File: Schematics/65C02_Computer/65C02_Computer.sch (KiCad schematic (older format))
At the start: 34 parts

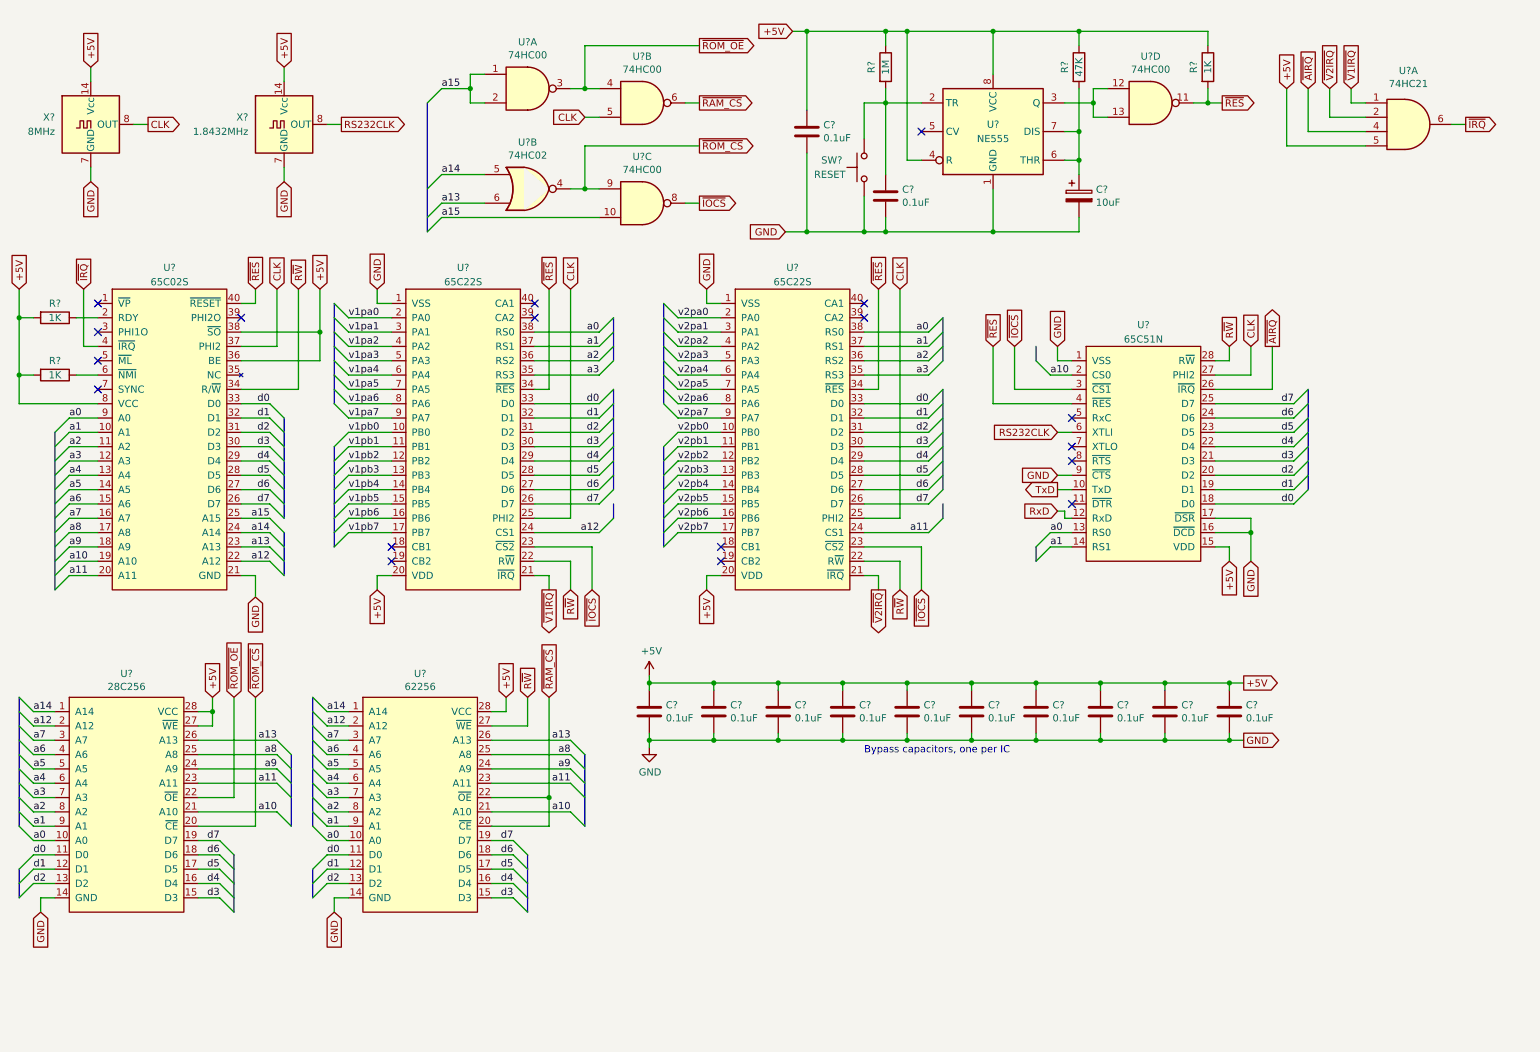
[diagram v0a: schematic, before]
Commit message: Added FT230X chip, moved peripherals to separate sheet
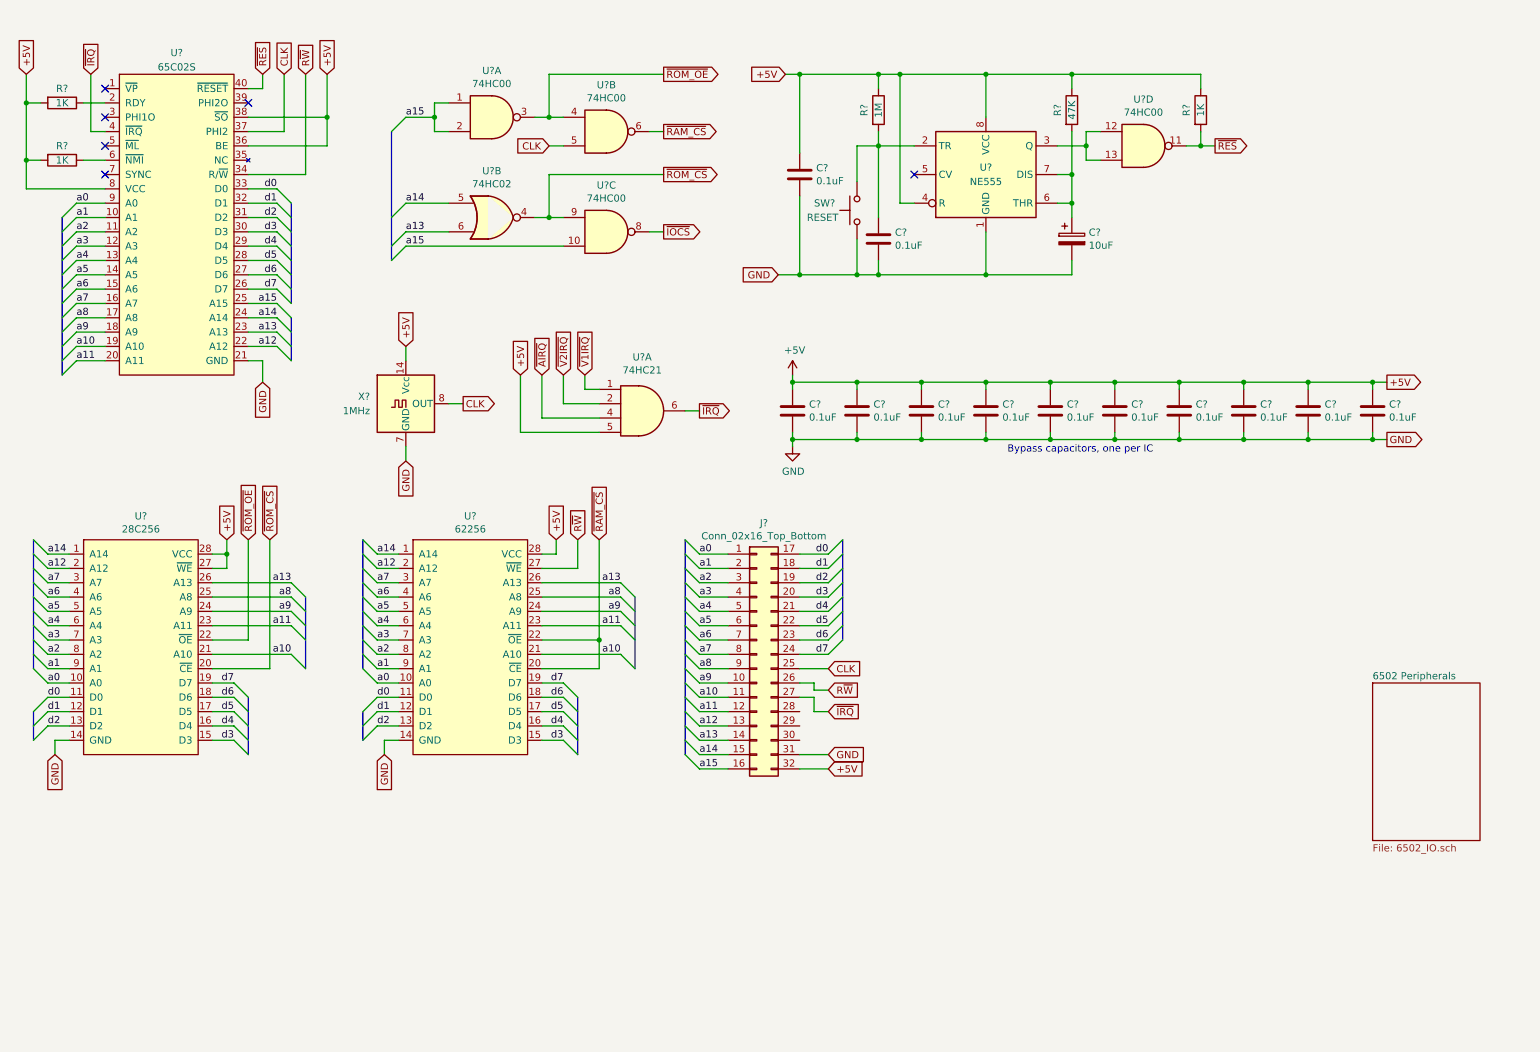
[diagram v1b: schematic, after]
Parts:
- removed U? (x2): 65C22S, Package_DIP:DIP-40_W15.24mm_Socket, symbol 6502:65C22S
- removed U?: 65C51N, Package_DIP:DIP-28_W15.24mm_Socket, symbol 6502:65C51N
- removed X?: 1.8432MHz, Oscillator:Oscillator_DIP-14, symbol Oscillator:ACO-xxxMHz
- added J?: Conn_02x16_Top_Bottom, Connector_PinSocket_2.54mm:PinSocket_2x16_P2.54mm_Vertical, symbol Connector_Generic:Conn_02x16_Top_Bottom
- X?: value 8MHz -> 1MHz
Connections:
- net +5V: now also J?.32 (Pin_32)
- net CLK: now also J?.25 (Pin_25)
- net GND: now also J?.31 (Pin_31)
- net R~W: now also J?.26 (Pin_26)
- net a0: now also J?.1 (Pin_1)
- net a1: now also J?.2 (Pin_2)
- net a10: now also J?.11 (Pin_11)
- net a11: now also J?.12 (Pin_12)
- net a12: now also J?.13 (Pin_13)
- net a13: now also J?.14 (Pin_14)
- net a14: now also J?.15 (Pin_15)
- net a15: now also J?.16 (Pin_16)
- net a2: now also J?.3 (Pin_3)
- net a3: now also J?.4 (Pin_4)
- net a4: now also J?.5 (Pin_5)
- net a5: now also J?.6 (Pin_6)
- net a6: now also J?.7 (Pin_7)
- net a7: now also J?.8 (Pin_8)
- net a8: now also J?.9 (Pin_9)
- net a9: now also J?.10 (Pin_10)
- net d0: now also J?.17 (Pin_17)
- net d1: now also J?.18 (Pin_18)
- net d2: now also J?.19 (Pin_19)
- net d3: now also J?.20 (Pin_20)
- net d4: now also J?.21 (Pin_21)
- net d5: now also J?.22 (Pin_22)
- net d6: now also J?.23 (Pin_23)
- net d7: now also J?.24 (Pin_24)
- net ~IRQ: now also J?.27 (Pin_27)
- no-connect marks 18 -> 6
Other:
- moved on the sheet: C?, R?, SW?, U?, U?A, U?B, U?C, U?D, X?

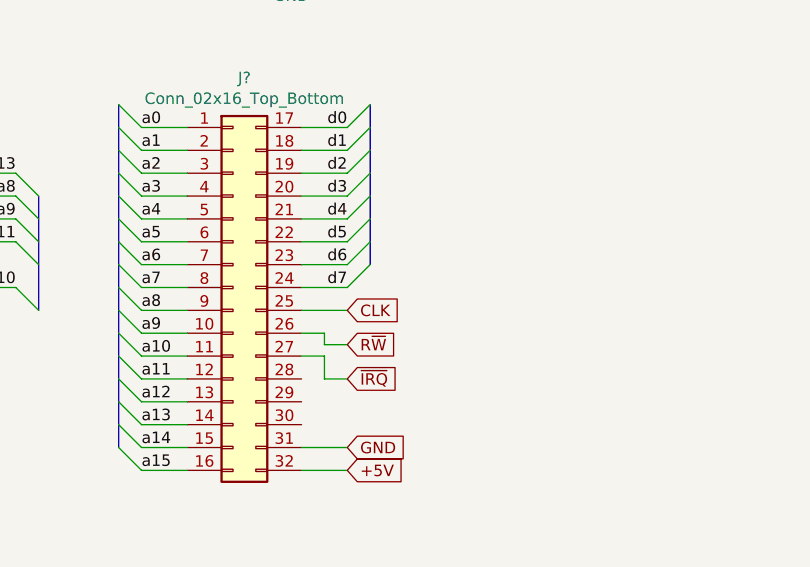
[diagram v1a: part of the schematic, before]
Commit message: Added two more lines to system port
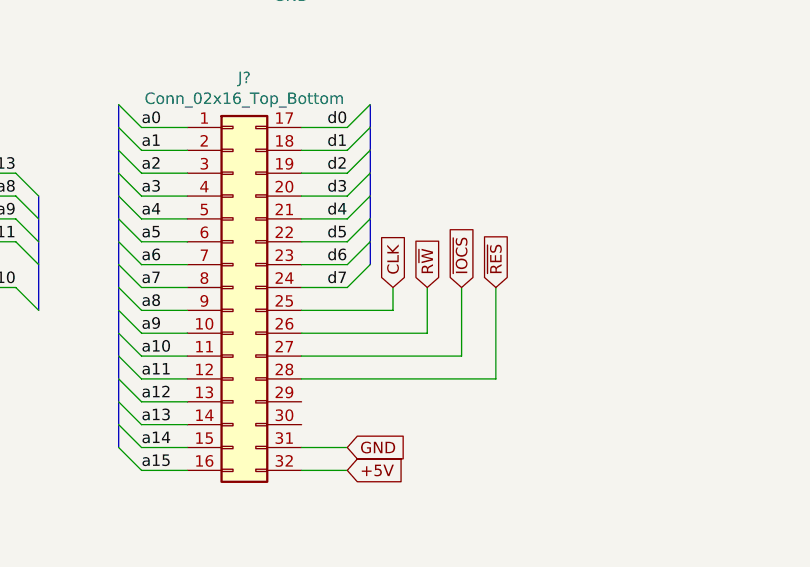
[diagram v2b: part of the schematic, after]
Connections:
- net ~IOCS: now also J?.27 (Pin_27)
- net ~IRQ: no longer J?.27 (Pin_27)
- net ~RES: now also J?.28 (Pin_28)
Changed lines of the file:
@@
 Entry Wire Line
 	6350 5050 6450 4950
-Text GLabel 6350 5150 2    50   Input ~ 0
+Text GLabel 6550 5050 1    50   Input ~ 0
 CLK
-Text GLabel 6350 5300 2    50   Input ~ 0
+Text GLabel 6700 5050 1    50   Input ~ 0
 R~W
-Text GLabel 6350 5450 2    50   Input ~ 0
-~IRQ
 Text GLabel 6350 5850 2    50   Input ~ 0
 +5V
@@
 	6150 5750 6350 5750
 Wire Wire Line
-	6150 5150 6350 5150
+	6550 5050 6550 5150
 Wire Wire Line
-	6150 5250 6250 5250
+	6550 5150 6150 5150
+Text GLabel 7000 5050 1    50   Input ~ 0
+~RES
+Text GLabel 6850 5050 1    50   Input ~ 0
+~IOCS
 Wire Wire Line
-	6250 5250 6250 5300
+	6700 5050 6700 5250
 Wire Wire Line
-	6250 5300 6350 5300
+	6700 5250 6150 5250
 Wire Wire Line
-	6150 5350 6250 5350
+	6850 5050 6850 5350
 Wire Wire Line
-	6250 5350 6250 5450
+	6850 5350 6150 5350
 Wire Wire Line
-	6250 5450 6350 5450
+	7000 5050 7000 5450
+Wire Wire Line
+	7000 5450 6150 5450
 Wire Bus Line
 	3100 5450 3100 5650

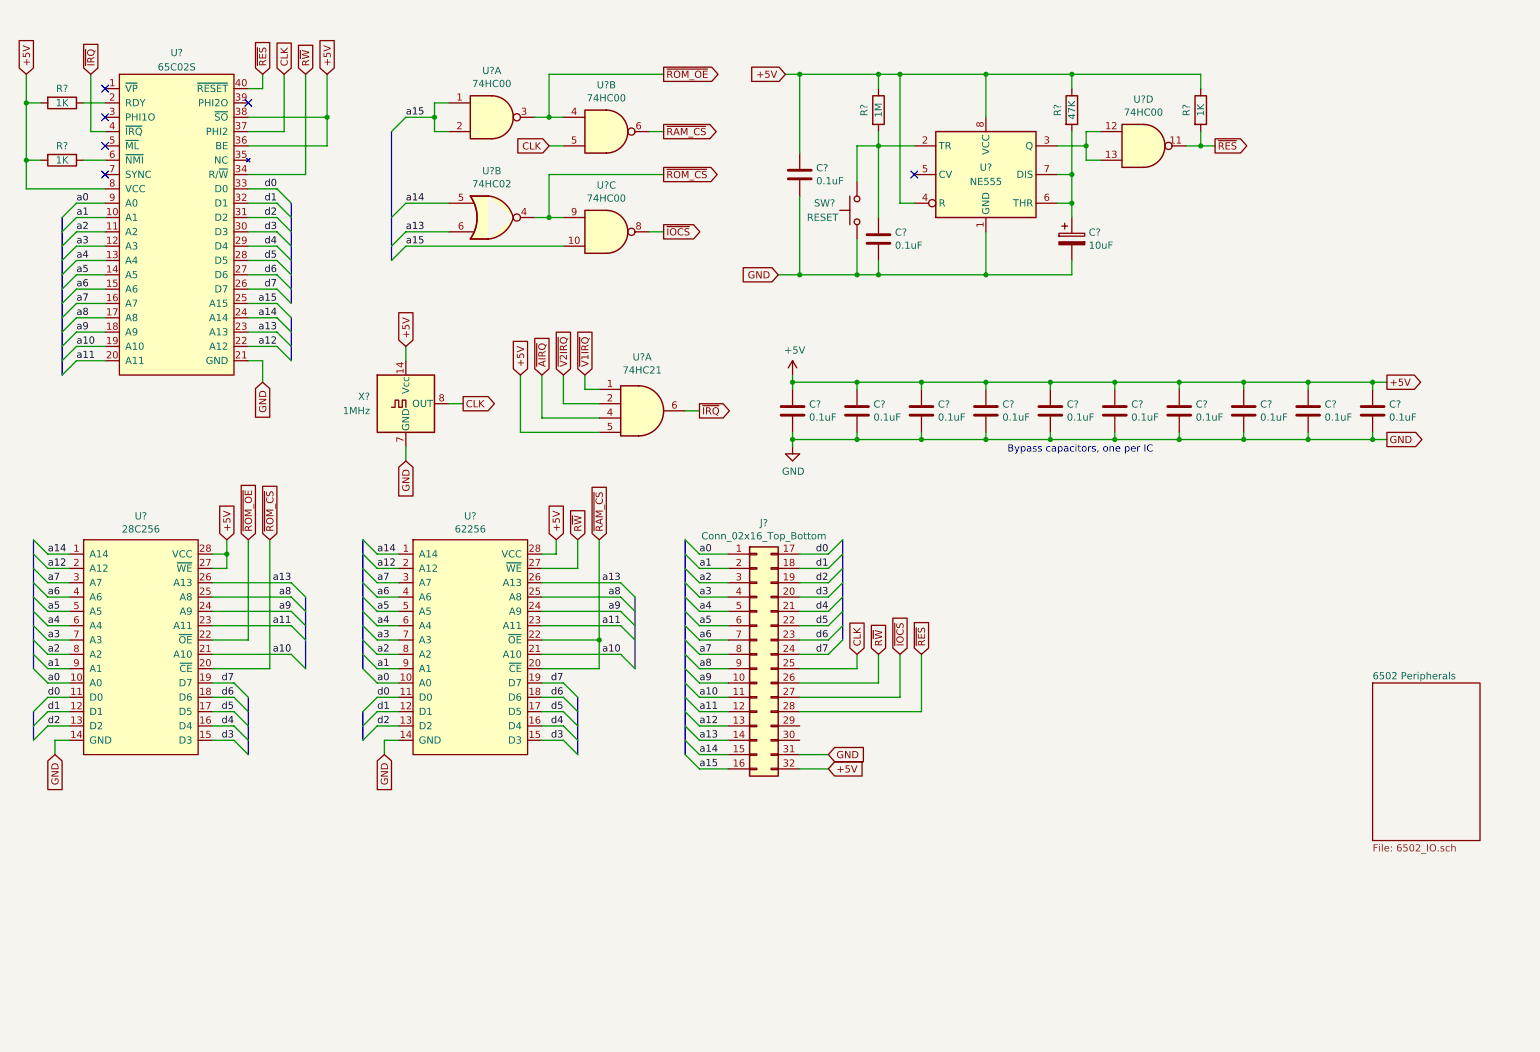
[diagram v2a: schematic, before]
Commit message: Added input IRQ pin, CLK jumper, changed pull-up values
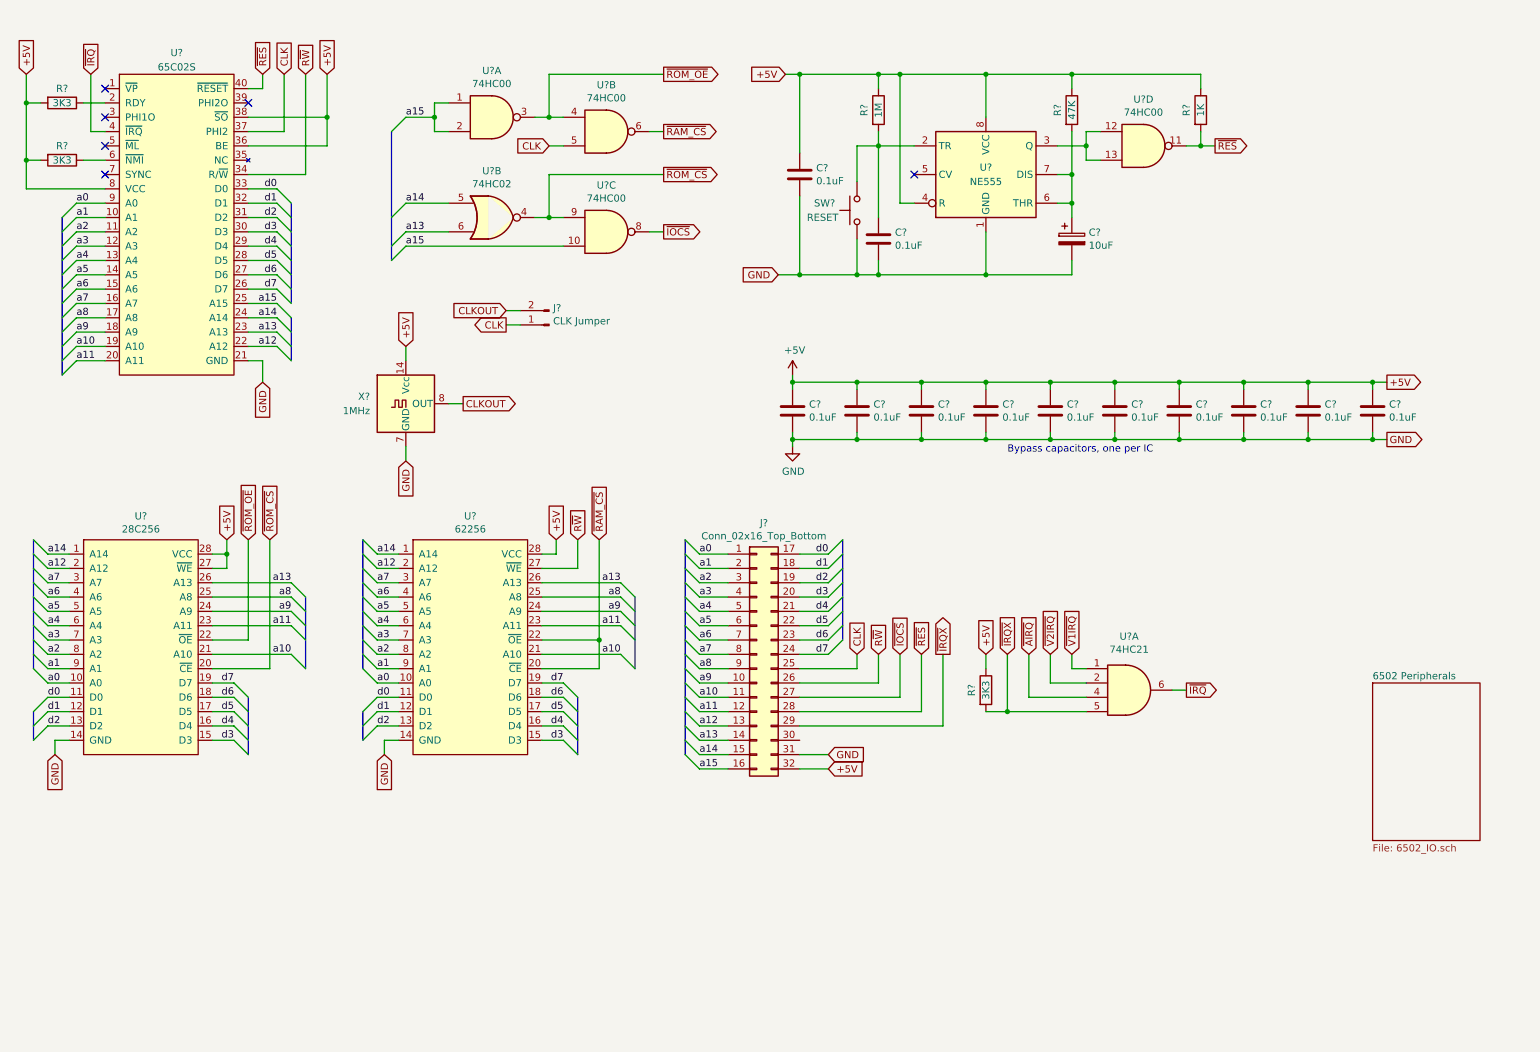
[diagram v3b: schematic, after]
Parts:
- added J?: CLK Jumper, Connector_PinHeader_2.54mm:PinHeader_1x02_P2.54mm_Vertical, symbol Connector:Conn_01x02_Male
- added R?: 3K3, Resistor_THT:R_Axial_DIN0207_L6.3mm_D2.5mm_P7.62mm_Horizontal, symbol Device:R
- R? (x2): value 1K -> 3K3
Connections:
- net +5V: now also R?.1; no longer U?.5
- net CLK: now also J?.1 (Pin_1); no longer X?.8 (OUT)
- net ~IRQX: now reaches J?.29 (Pin_29)
- net ~IRQX: now also U?.5, R?.2
- new net CLKOUT: J?.2 (Pin_2), X?.8 (OUT)
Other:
- moved on the sheet: U?A
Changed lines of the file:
@@
 	3400 3000 3400 2900
 Text GLabel 3800 3300 2    50   Output ~ 0
-CLK
+CLKOUT
 Wire Wire Line
 	3700 3300 3800 3300
@@
 P 1000 1600
 F 0 "R?" V 900 1600 50  0000 C CNN
-F 1 "1K" V 1000 1600 50  0000 C CNN
+F 1 "3K3" V 1000 1600 50  0000 C CNN
 F 2 "Resistor_THT:R_Axial_DIN0207_L6.3mm_D2.5mm_P7.62mm_Horizontal" V 930 1600 50  0001 C CNN
 F 3 "~" H 1000 1600 50  0001 C CNN
@@
 P 1000 1200
 F 0 "R?" V 900 1200 50  0000 C CNN
-F 1 "1K" V 1000 1200 50  0000 C CNN
+F 1 "3K3" V 1000 1200 50  0000 C CNN
 F 2 "Resistor_THT:R_Axial_DIN0207_L6.3mm_D2.5mm_P7.62mm_Horizontal" V 930 1200 50  0001 C CNN
 F 3 "~" H 1000 1200 50  0001 C CNN
@@
 L 74xx:74LS21 U?
 U 1 1 5E23A6D1
-P 5050 3350
-F 0 "U?" H 5050 3725 50  0000 C CNN
-F 1 "74HC21" H 5050 3634 50  0000 C CNN
-F 2 "Package_DIP:DIP-14_W7.62mm_Socket" H 5050 3350 50  0001 C CNN
-F 3 "http://www.ti.com/lit/gpn/sn74LS21" H 5050 3350 50  0001 C CNN
-	1    5050 3350
-	1    0    0    -1
-$EndComp
-Text GLabel 4650 3100 1    50   Input ~ 0
+P 8450 5300
+F 0 "U?" H 8450 5675 50  0000 C CNN
+F 1 "74HC21" H 8450 5584 50  0000 C CNN
+F 2 "Package_DIP:DIP-14_W7.62mm_Socket" H 8450 5300 50  0001 C CNN
+F 3 "http://www.ti.com/lit/gpn/sn74LS21" H 8450 5300 50  0001 C CNN
+	1    8450 5300
+	1    0    0    -1
+$EndComp
+Text GLabel 8050 5050 1    50   Input ~ 0
 ~V1IRQ
-Text GLabel 4500 3100 1    50   Input ~ 0
+Text GLabel 7900 5050 1    50   Input ~ 0
 ~V2IRQ
-Text GLabel 4350 3100 1    50   Input ~ 0
+Text GLabel 7750 5050 1    50   Input ~ 0
 ~AIRQ
-Text GLabel 4200 3100 1    50   Input ~ 0
-+5V
-Wire Wire Line
-	4650 3100 4650 3200
-Wire Wire Line
-	4650 3200 4750 3200
-Wire Wire Line
-	4500 3100 4500 3300
-Wire Wire Line
-	4500 3300 4750 3300
-Wire Wire Line
-	4350 3100 4350 3400
-Wire Wire Line
-	4350 3400 4750 3400
-Wire Wire Line
-	4200 3100 4200 3500
-Wire Wire Line
-	4200 3500 4750 3500
-Text GLabel 5450 3350 2    50   Output ~ 0
+Wire Wire Line
+	8050 5050 8050 5150
+Wire Wire Line
+	8050 5150 8150 5150
+Wire Wire Line
+	7900 5050 7900 5250
+Wire Wire Line
+	7900 5250 8150 5250
+Wire Wire Line
+	7750 5050 7750 5350
+Wire Wire Line
+	7750 5350 8150 5350
+Wire Wire Line
+	7600 5050 7600 5450
+Wire Wire Line
+	7600 5450 8150 5450
+Text GLabel 8850 5300 2    50   Output ~ 0
 ~IRQ
 Wire Wire Line
-	5350 3350 5450 3350
+	8750 5300 8850 5300
 Wire Wire Line
 	2300 1300 2850 1300
@@
 Wire Wire Line
 	7000 5450 6150 5450
+Text GLabel 7150 5050 1    50   Output ~ 0
+~IRQX
+Wire Wire Line
+	6150 5550 7150 5550
+Wire Wire Line
+	7150 5550 7150 5050
+Text GLabel 7600 5050 1    50   Input ~ 0
+~IRQX
+Text GLabel 7450 5050 1    50   Input ~ 0
++5V
+$Comp
+L Device:R R?
+U 1 1 5E451554
+P 7450 5300
+F 0 "R?" V 7350 5300 50  0000 C CNN
+F 1 "3K3" V 7450 5300 50  0000 C CNN
+F 2 "Resistor_THT:R_Axial_DIN0207_L6.3mm_D2.5mm_P7.62mm_Horizontal" V 7380 5300 50  0001 C CNN
+F 3 "~" H 7450 5300 50  0001 C CNN
+	1    7450 5300
+	1    0    0    -1
+$EndComp
+Wire Wire Line
+	7450 5050 7450 5150
+Wire Wire Line
+	7450 5450 7600 5450
+Connection ~ 7600 5450
+$Comp
+L Connector:Conn_01x02_Male J?
+U 1 1 5E49655D
+P 4400 2750
+F 0 "J?" H 4372 2632 50  0000 R CNN
+F 1 "CLK Jumper" H 4372 2723 50  0000 R CNN
+F 2 "Connector_PinHeader_2.54mm:PinHeader_1x02_P2.54mm_Vertical" H 4400 2750 50  0001 C CNN
+F 3 "~" H 4400 2750 50  0001 C CNN
+	1    4400 2750
+	-1   0    0    1
+$EndComp
+Text GLabel 4100 2650 0    50   Input ~ 0
+CLKOUT
+Text GLabel 4100 2750 0    50   Output ~ 0
+CLK
+Wire Wire Line
+	4100 2650 4200 2650
+Wire Wire Line
+	4100 2750 4200 2750
 Wire Bus Line
 	3100 5450 3100 5650
